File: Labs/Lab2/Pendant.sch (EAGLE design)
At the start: 24 parts

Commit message: Updated Pendant design for 2019
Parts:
- removed R7, R8, R9: (no value), rcl:R-US_R1206
- added LED10, LED11, LED12, LED13, LED14, LED15, LED16, LED17, LED18, LED19, LED20, LED21, LED22, LED23, LED24, LED9: (no value), led:LEDCHIPLED_1206
- added LSP1, LSP10, LSP11, LSP12, LSP13, LSP14, LSP15, LSP16, LSP17, LSP18, LSP19, LSP2, LSP20, LSP21, LSP22, LSP23, LSP24, LSP3, LSP4, LSP5, LSP6, LSP7, LSP8, LSP9: LSP10, solpad-mod:LSP10
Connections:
- removed net D1: MSP430.8, R1.1
- removed net D2: MSP430.9, R2.1
- removed net D3: MSP430.10, R3.1
- removed net D4: MSP430.11, R4.1
- removed net D5: MSP430.12, R5.1
- removed net D6: MSP430.13, R6.1
- removed net D7: MSP430.14, R7.1
- removed net D8: MSP430.15, R8.1
- removed net N$14: C2.2, MSP430.4, R9.2, S1.2
- removed net N$2: LED2.A, R2.2
- new net CA1: LED1.C, LED13.C, LED19.C, LED7.C, R1.2
- new net CA2: LED14.C, LED2.C, LED20.C, LED8.C, R2.2
- new net CA3: LED15.C, LED21.C, LED3.C, LED9.C, R3.2
- new net CA4: LED10.C, LED16.C, LED22.C, LED4.C, R4.2
- new net CA5: LED11.C, LED17.C, LED23.C, LED5.C, R5.2
- new net CA6: LED12.C, LED18.C, LED24.C, LED6.C, R6.2
- new net CAP1: MSP430.19
- new net CAP2: MSP430.18
- new net CB1: LED1.A, LED2.A, LED3.A, LED4.A, LED5.A, LED6.A, LSP1.MP, LSP2.MP, LSP3.MP, LSP4.MP, LSP5.MP, LSP6.MP, MSP430.9
- new net CB2: LED10.A, LED11.A, LED12.A, LED7.A, LED8.A, LED9.A, LSP10.MP, LSP11.MP, LSP12.MP, LSP7.MP, LSP8.MP, LSP9.MP, MSP430.10
- new net CB3: LED13.A, LED14.A, LED15.A, LED16.A, LED17.A, LED18.A, LSP13.MP, LSP14.MP, LSP15.MP, LSP16.MP, LSP17.MP, LSP18.MP, MSP430.12
- new net CB4: LED19.A, LED20.A, LED21.A, LED22.A, LED23.A, LED24.A, LSP19.MP, LSP20.MP, LSP21.MP, LSP22.MP, LSP23.MP, LSP24.MP, MSP430.13
- new net N$9: MSP430.14
- new net SWITCH1: C2.2, MSP430.15, S1.1
- net GND: now also S1.2; no longer LED1.C, LED2.C, LED3.C, LED4.C, LED5.C, LED6.C, LED7.C, LED8.C, S1.1
- net N$1: now also MSP430.8; no longer LED1.A, R1.2
- net N$3: now also MSP430.2, R1.1; no longer LED3.A, R3.2
- net N$4: now also MSP430.3, R2.1; no longer LED4.A, R4.2
- net N$5: now also MSP430.4, R3.1; no longer LED5.A, R5.2
- net N$6: now also MSP430.5, R4.1; no longer LED6.A, R6.2
- net N$7: now also MSP430.6, R5.1; no longer LED7.A, R7.2
- net N$8: now also MSP430.7, R6.1; no longer LED8.A, R8.2
- net VDD: no longer R9.1

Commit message: Updated pendant for 2021 (tic tac toe)
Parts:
- removed LED1, LED10, LED11, LED12, LED13, LED14, LED15, LED16, LED17, LED18, LED19, LED2, LED20, LED21, LED22, LED23, LED24, LED3, LED4, LED5, LED6, LED7, LED8, LED9: (no value), led:LEDCHIPLED_1206
- removed LSP1, LSP10, LSP11, LSP12, LSP13, LSP14, LSP15, LSP16, LSP17, LSP18, LSP19, LSP2, LSP20, LSP21, LSP22, LSP23, LSP24, LSP3, LSP4, LSP5, LSP6, LSP7, LSP8, LSP9: LSP10, solpad-mod:LSP10
- removed R1, R2, R3, R4, R5, R6: (no value), rcl:R-US_R1206
- added C3: 470nF, rcl:C-USC1206
- added R_BLU, R_GRN, R_RED: (no value), rcl:R-US_R1206
- added S2: MOMENTARY-SWITCH-SPST-PTH-6.0MM, SparkFun-Switches:MOMENTARY-SWITCH-SPST-PTH-6.0MM
- added U$1, U$2, U$3, U$4, U$5, U$6, U$7, U$8, U$9: RGBLED, RGB-LED:RGBLED
- renumbered R10 to RPROG
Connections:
- removed net CAP1: MSP430.19
- removed net CAP2: MSP430.18
- removed net CB1: LED1.A, LED2.A, LED3.A, LED4.A, LED5.A, LED6.A, LSP1.MP, LSP2.MP, LSP3.MP, LSP4.MP, LSP5.MP, LSP6.MP, MSP430.9
- removed net CB2: LED10.A, LED11.A, LED12.A, LED7.A, LED8.A, LED9.A, LSP10.MP, LSP11.MP, LSP12.MP, LSP7.MP, LSP8.MP, LSP9.MP, MSP430.10
- removed net CB3: LED13.A, LED14.A, LED15.A, LED16.A, LED17.A, LED18.A, LSP13.MP, LSP14.MP, LSP15.MP, LSP16.MP, LSP17.MP, LSP18.MP, MSP430.12
- removed net CB4: LED19.A, LED20.A, LED21.A, LED22.A, LED23.A, LED24.A, LSP19.MP, LSP20.MP, LSP21.MP, LSP22.MP, LSP23.MP, LSP24.MP, MSP430.13
- removed net N$3: MSP430.2, R1.1
- removed net N$4: MSP430.3, R2.1
- removed net N$5: MSP430.4, R3.1
- removed net N$6: MSP430.5, R4.1
- removed net N$7: MSP430.6, R5.1
- removed net N$8: MSP430.7, R6.1
- removed net N$9: MSP430.14
- removed net SWITCH1: C2.2, MSP430.15, S1.1
- new net BLUE: R_BLU.2, U$1.3, U$2.3, U$3.3, U$4.3, U$5.3, U$6.3, U$7.3, U$8.3, U$9.3
- new net CA0: MSP430.2, U$1.1
- new net CA7: MSP430.15, U$8.1
- new net CA8: MSP430.8, U$9.1
- new net CB0: MSP430.19, R_BLU.1
- new net GREEN: R_GRN.2, U$1.4, U$2.4, U$3.4, U$4.4, U$5.4, U$6.4, U$7.4, U$8.4, U$9.4
- new net N$2: MSP430.13, R_GRN.1
- new net RED: R_RED.2, U$1.2, U$2.2, U$3.2, U$4.2, U$5.2, U$6.2, U$7.2, U$8.2, U$9.2
- new net SW0: C2.2, MSP430.9, S1.1
- new net SW1: C3.2, MSP430.10, S2.1
- net CA1: now also MSP430.3, U$2.1; no longer LED1.C, LED13.C, LED19.C, LED7.C, R1.2
- net CA2: now also MSP430.4, U$3.1; no longer LED14.C, LED2.C, LED20.C, LED8.C, R2.2
- net CA3: now also MSP430.5, U$4.1; no longer LED15.C, LED21.C, LED3.C, LED9.C, R3.2
- net CA4: now also MSP430.6, U$5.1; no longer LED10.C, LED16.C, LED22.C, LED4.C, R4.2
- net CA5: now also MSP430.7, U$6.1; no longer LED11.C, LED17.C, LED23.C, LED5.C, R5.2
- net CA6: now also MSP430.14, U$7.1; no longer LED12.C, LED18.C, LED24.C, LED6.C, R6.2
- net GND: now also C3.1, S2.2
- net N$1: now also MSP430.12, R_RED.1; no longer MSP430.8

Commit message: Restored original 2020 pendant in directory, made a new directory for 2021 fabbed pendant, and a directory for Bonus PCB.
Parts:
- removed C3: 470nF, rcl:C-USC1206
- removed R_BLU, R_GRN, R_RED: (no value), rcl:R-US_R1206
- removed S2: MOMENTARY-SWITCH-SPST-PTH-6.0MM, SparkFun-Switches:MOMENTARY-SWITCH-SPST-PTH-6.0MM
- removed U$1, U$2, U$3, U$4, U$5, U$6, U$7, U$8, U$9: RGBLED, RGB-LED:RGBLED
- added LED1, LED10, LED11, LED12, LED13, LED14, LED15, LED16, LED17, LED18, LED19, LED2, LED20, LED21, LED22, LED23, LED24, LED3, LED4, LED5, LED6, LED7, LED8, LED9: (no value), led:LEDCHIPLED_1206
- added LSP1, LSP10, LSP11, LSP12, LSP13, LSP14, LSP15, LSP16, LSP17, LSP18, LSP19, LSP2, LSP20, LSP21, LSP22, LSP23, LSP24, LSP3, LSP4, LSP5, LSP6, LSP7, LSP8, LSP9: LSP10, solpad-mod:LSP10
- added R1, R2, R3, R4, R5, R6: (no value), rcl:R-US_R1206
- renumbered RPROG to R10
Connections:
- removed net BLUE: R_BLU.2, U$1.3, U$2.3, U$3.3, U$4.3, U$5.3, U$6.3, U$7.3, U$8.3, U$9.3
- removed net CA0: MSP430.2, U$1.1
- removed net CA7: MSP430.15, U$8.1
- removed net CA8: MSP430.8, U$9.1
- removed net CB0: MSP430.19, R_BLU.1
- removed net GREEN: R_GRN.2, U$1.4, U$2.4, U$3.4, U$4.4, U$5.4, U$6.4, U$7.4, U$8.4, U$9.4
- removed net N$2: MSP430.13, R_GRN.1
- removed net RED: R_RED.2, U$1.2, U$2.2, U$3.2, U$4.2, U$5.2, U$6.2, U$7.2, U$8.2, U$9.2
- removed net SW0: C2.2, MSP430.9, S1.1
- removed net SW1: C3.2, MSP430.10, S2.1
- new net CAP1: MSP430.19
- new net CAP2: MSP430.18
- new net CB1: LED1.A, LED2.A, LED3.A, LED4.A, LED5.A, LED6.A, LSP1.MP, LSP2.MP, LSP3.MP, LSP4.MP, LSP5.MP, LSP6.MP, MSP430.9
- new net CB2: LED10.A, LED11.A, LED12.A, LED7.A, LED8.A, LED9.A, LSP10.MP, LSP11.MP, LSP12.MP, LSP7.MP, LSP8.MP, LSP9.MP, MSP430.10
- new net CB3: LED13.A, LED14.A, LED15.A, LED16.A, LED17.A, LED18.A, LSP13.MP, LSP14.MP, LSP15.MP, LSP16.MP, LSP17.MP, LSP18.MP, MSP430.12
- new net CB4: LED19.A, LED20.A, LED21.A, LED22.A, LED23.A, LED24.A, LSP19.MP, LSP20.MP, LSP21.MP, LSP22.MP, LSP23.MP, LSP24.MP, MSP430.13
- new net N$3: MSP430.2, R1.1
- new net N$4: MSP430.3, R2.1
- new net N$5: MSP430.4, R3.1
- new net N$6: MSP430.5, R4.1
- new net N$7: MSP430.6, R5.1
- new net N$8: MSP430.7, R6.1
- new net N$9: MSP430.14
- new net SWITCH1: C2.2, MSP430.15, S1.1
- net CA1: now also LED1.C, LED13.C, LED19.C, LED7.C, R1.2; no longer MSP430.3, U$2.1
- net CA2: now also LED14.C, LED2.C, LED20.C, LED8.C, R2.2; no longer MSP430.4, U$3.1
- net CA3: now also LED15.C, LED21.C, LED3.C, LED9.C, R3.2; no longer MSP430.5, U$4.1
- net CA4: now also LED10.C, LED16.C, LED22.C, LED4.C, R4.2; no longer MSP430.6, U$5.1
- net CA5: now also LED11.C, LED17.C, LED23.C, LED5.C, R5.2; no longer MSP430.7, U$6.1
- net CA6: now also LED12.C, LED18.C, LED24.C, LED6.C, R6.2; no longer MSP430.14, U$7.1
- net GND: no longer C3.1, S2.2
- net N$1: now also MSP430.8; no longer MSP430.12, R_RED.1

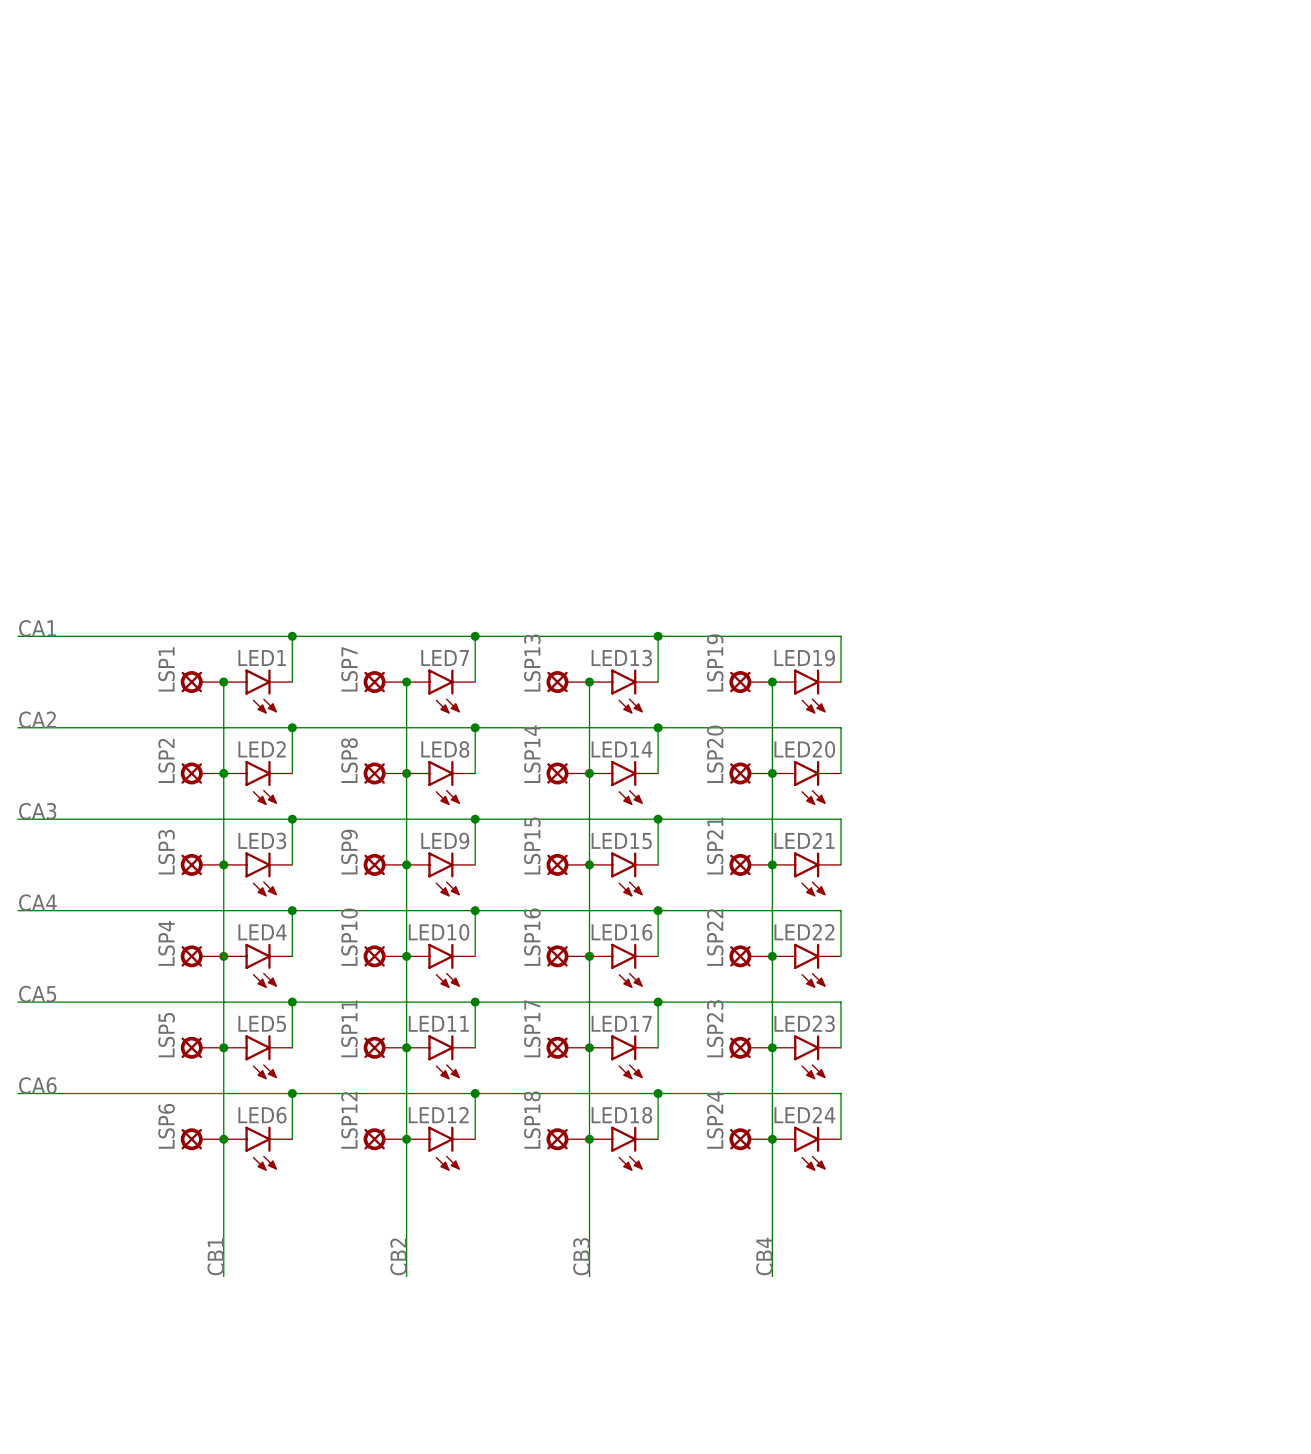
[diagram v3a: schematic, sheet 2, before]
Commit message: Pendant for 2022 is a 5x7 LED array
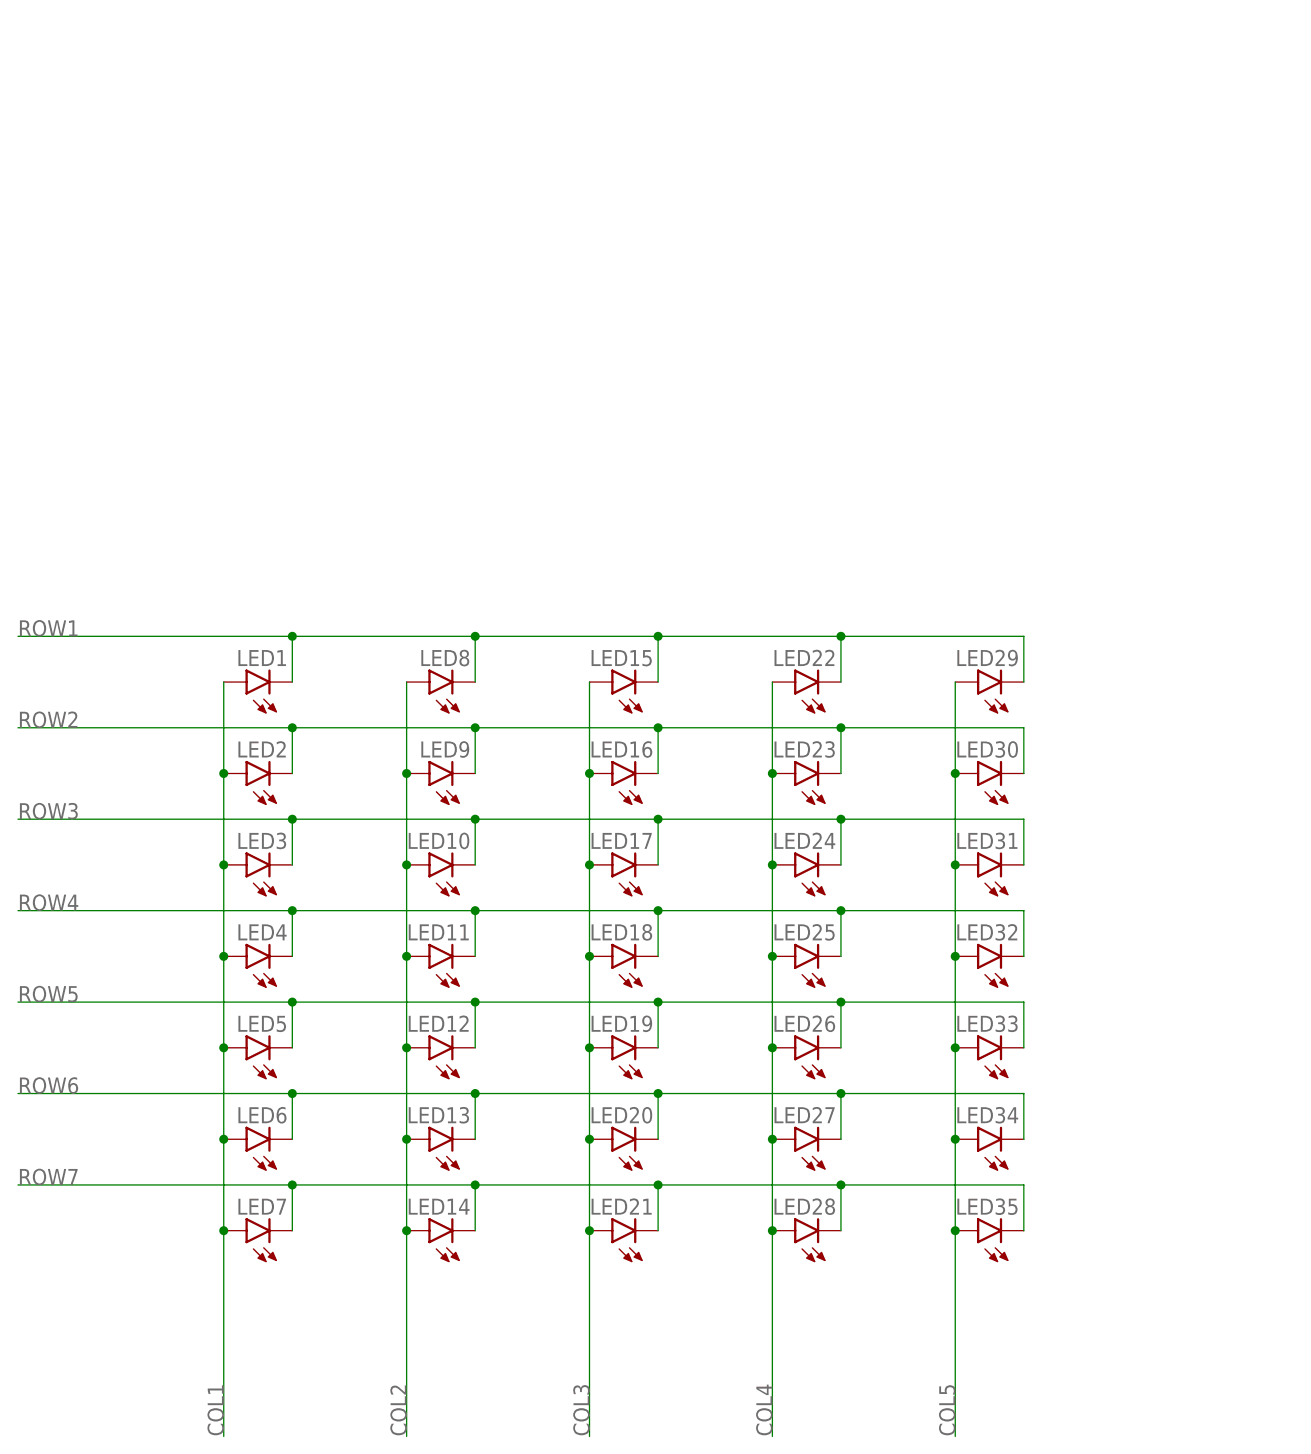
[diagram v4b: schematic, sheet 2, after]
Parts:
- removed BAT1: 20mm coincell, Battery:BATTERYFOB
- removed LSP1, LSP10, LSP11, LSP12, LSP13, LSP14, LSP15, LSP16, LSP17, LSP18, LSP19, LSP2, LSP20, LSP21, LSP22, LSP23, LSP24, LSP3, LSP4, LSP5, LSP6, LSP7, LSP8, LSP9: LSP10, solpad-mod:LSP10
- removed S1: MOMENTARY-SWITCH-SPST-PTH-6.0MM, SparkFun-Switches:MOMENTARY-SWITCH-SPST-PTH-6.0MM
- added BT1: BC2AAAPC, BC2AAAPC:BC2AAAPC
- added C3: 100u, rcl:C-USC1206
- added C4: 47nF, rcl:C-USC0603
- added JP2, JP3: (no value), Pendant:M04LOCK
- added LED25, LED26, LED27, LED28, LED29, LED30, LED31, LED32, LED33, LED34, LED35: (no value), led:LEDSML1206
- added R7: (no value), rcl:R-US_R0402
- added SW1, SW2: SWITCH_SPSTSMD, ELEC327:SWITCH_SPSTSMD
- added U$1: SWITCH_DPDT, ELEC327:SWITCH_DPDT
- C1: value 10u -> 1u; device rcl:C-USC1206 -> rcl:C-USC0603
- C2: value 470nF -> 47nF; device rcl:C-USC1206 -> rcl:C-USC0603
- LED1, LED10, LED11, LED12, LED13, LED14, LED15, LED16, LED17, LED18, LED19, LED2, LED20, LED21, LED22, LED23, LED24, LED3, LED4, LED5, LED6, LED7, LED8, LED9: device led:LEDCHIPLED_1206 -> led:LEDSML1206
- R1, R10, R2, R3, R4, R5, R6: device rcl:R-US_R1206 -> rcl:R-US_R0402
- renumbered JP1 to TRVG
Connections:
- removed net CA1: LED1.C, LED13.C, LED19.C, LED7.C, R1.2
- removed net CA2: LED14.C, LED2.C, LED20.C, LED8.C, R2.2
- removed net CA3: LED15.C, LED21.C, LED3.C, LED9.C, R3.2
- removed net CA4: LED10.C, LED16.C, LED22.C, LED4.C, R4.2
- removed net CA5: LED11.C, LED17.C, LED23.C, LED5.C, R5.2
- removed net CA6: LED12.C, LED18.C, LED24.C, LED6.C, R6.2
- removed net CAP1: MSP430.19
- removed net CAP2: MSP430.18
- removed net CB1: LED1.A, LED2.A, LED3.A, LED4.A, LED5.A, LED6.A, LSP1.MP, LSP2.MP, LSP3.MP, LSP4.MP, LSP5.MP, LSP6.MP, MSP430.9
- removed net CB2: LED10.A, LED11.A, LED12.A, LED7.A, LED8.A, LED9.A, LSP10.MP, LSP11.MP, LSP12.MP, LSP7.MP, LSP8.MP, LSP9.MP, MSP430.10
- removed net CB3: LED13.A, LED14.A, LED15.A, LED16.A, LED17.A, LED18.A, LSP13.MP, LSP14.MP, LSP15.MP, LSP16.MP, LSP17.MP, LSP18.MP, MSP430.12
- removed net CB4: LED19.A, LED20.A, LED21.A, LED22.A, LED23.A, LED24.A, LSP19.MP, LSP20.MP, LSP21.MP, LSP22.MP, LSP23.MP, LSP24.MP, MSP430.13
- removed net N$9: MSP430.14
- new net COL1: LED1.A, LED2.A, LED3.A, LED4.A, LED5.A, LED6.A, LED7.A, MSP430.8
- new net COL2: LED10.A, LED11.A, LED12.A, LED13.A, LED14.A, LED8.A, LED9.A, MSP430.9
- new net COL3: LED15.A, LED16.A, LED17.A, LED18.A, LED19.A, LED20.A, LED21.A, MSP430.10
- new net COL4: LED22.A, LED23.A, LED24.A, LED25.A, LED26.A, LED27.A, LED28.A, MSP430.11
- new net COL5: LED29.A, LED30.A, LED31.A, LED32.A, LED33.A, LED34.A, LED35.A, MSP430.12
- new net N$2: BT1.+, U$1.2, U$1.5
- new net ROW1: LED1.C, LED15.C, LED22.C, LED29.C, LED8.C, R1.2
- new net ROW2: LED16.C, LED2.C, LED23.C, LED30.C, LED9.C, R2.2
- new net ROW3: LED10.C, LED17.C, LED24.C, LED3.C, LED31.C, R3.2
- new net ROW4: LED11.C, LED18.C, LED25.C, LED32.C, LED4.C, R4.2
- new net ROW5: LED12.C, LED19.C, LED26.C, LED33.C, LED5.C, R5.2
- new net ROW6: LED13.C, LED20.C, LED27.C, LED34.C, LED6.C, R6.2
- new net ROW7: LED14.C, LED21.C, LED28.C, LED35.C, LED7.C, R7.2
- new net SIG1: JP2.2, JP3.2, MSP430.19
- new net SIG2: JP2.3, JP3.3, MSP430.18
- new net SWITCH2: C2.2, MSP430.15, SW2.3
- net GND: now also BT1.-, C3.2, C4.1, JP2.1, JP3.1, SW1.1, SW2.1, TRVG.1; no longer BAT1.-, S1.2, TRVG.4
- net N$1: now also MSP430.14, R7.1; no longer MSP430.8
- net SWITCH1: now also C4.2, MSP430.13, SW1.3; no longer C2.2, MSP430.15, S1.1
- net TEST: now also TRVG.4; no longer TRVG.2
- net VDD: now also C3.1, JP2.4, JP3.4, TRVG.2, U$1.1, U$1.4; no longer BAT1.+, TRVG.1
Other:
- moved on the sheet: C2, LED10, LED11, LED12, LED13, LED14, LED15, LED16, LED17, LED18, LED19, LED20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
